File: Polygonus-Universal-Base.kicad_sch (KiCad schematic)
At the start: 11 parts, among them J1 Conn_02x04_Top_Bottom, J4 Polygonus_Plugs, J5 Conn_02x04_Top_Bottom, U1 f042_wideband_module, U14 f042_wideband_module

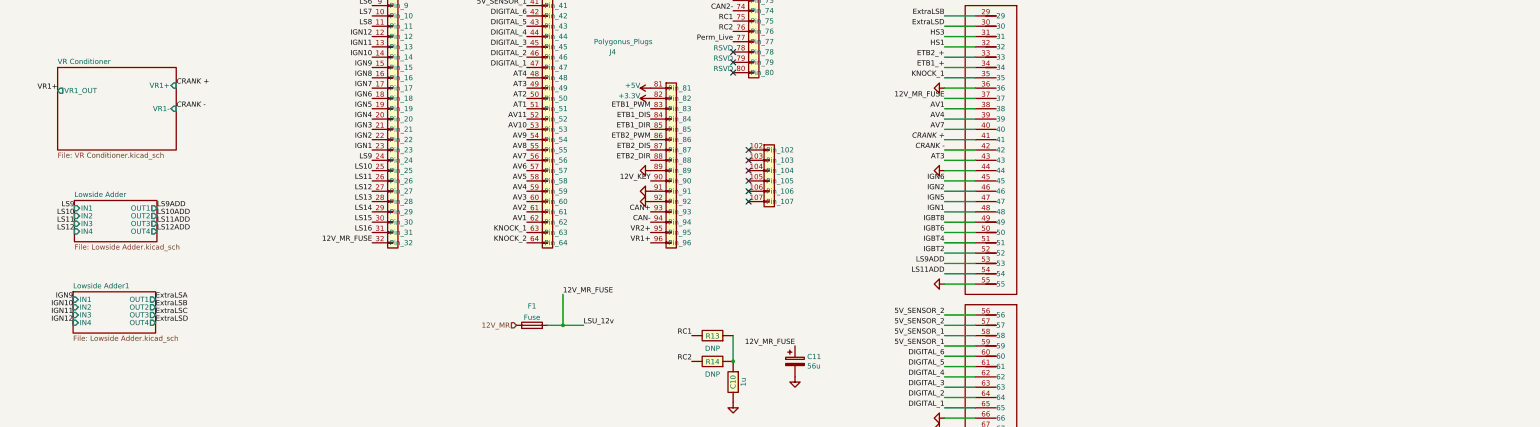
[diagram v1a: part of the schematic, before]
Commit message: Add freewheel diodes, power pins explanation comment
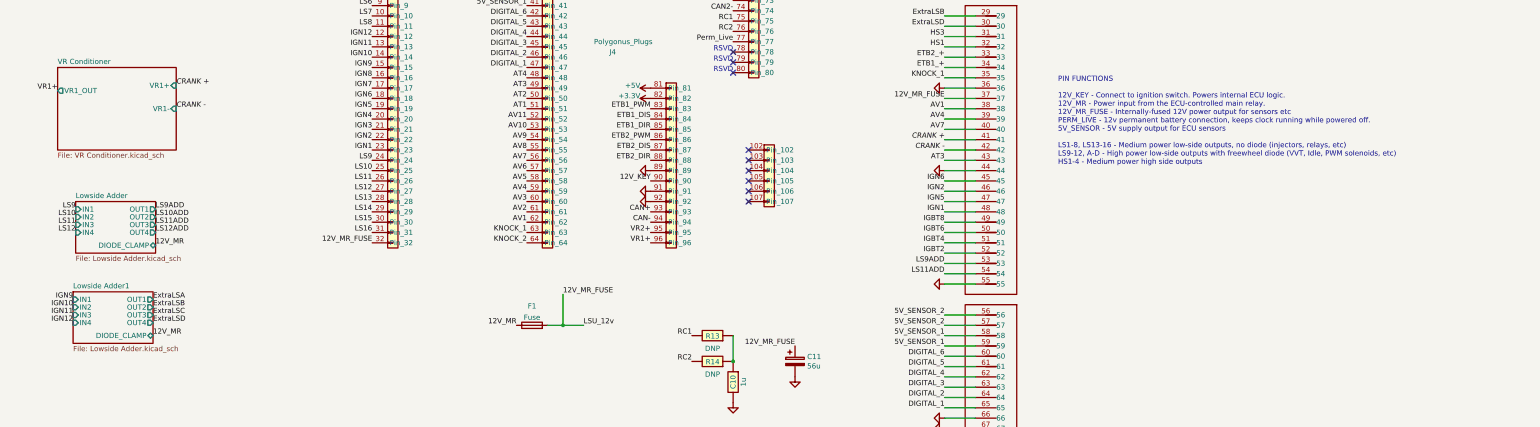
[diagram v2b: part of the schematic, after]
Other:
- sheet Lowside Adder ports: added DIODE_CLAMP; removed none
- sheet Lowside Adder1 ports: added DIODE_CLAMP; removed none
- note added: "PIN FUNCTIONS 12V_KEY - Connect to ignition switch. Powers internal ECU logic. 12V_MR - Power input from the ECU-controlled main relay. 12V_MR_FUSE - Internally-fused 12V power output for sensors etc PERM_LIVE - 12v permanent battery connection, keeps clock running while powered off. 5V_SENSOR - 5V supply output for ECU sensors LS1-8, LS13-16 - Medium power low-side outputs, no diode (injectors, 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"
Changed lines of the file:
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@@
     (stroke (width 0) (type default))
   )
+  (text "PIN FUNCTIONS\n\n12V_KEY - Connect to ignition switch. Powers internal ECU logic.\n12V_MR - Power input from the ECU-controlled main relay.\n12V_MR_FUSE - Internally-fused 12V power output for sensors etc\nPERM_LIVE - 12v permanent battery connection, keeps clock running while powered off.\n5V_SENSOR - 5V supply output for ECU sensors\n\nLS1-8, LS13-16 - Medium power low-side outputs, no diode (injectors, relays, etc)\nLS9-12, A-D - High power low-side outputs with freewheel diode (VVT, Idle, PWM solenoids, etc)\nHS1-4 - Medium power high side outputs"
+    (at 299.72 144.78 0)
+    (effects (font (size 1.27 1.27)) (justify left bottom))
+  )
   (text "RSVD" (at 168.91 97.79 0)
     (effects (font (size 1.27 1.27)) (justify right bottom))
@@
     (effects (font (size 1.27 1.27)) (justify right bottom))
   )
-  (label "LS11" (at 57.4793 159.1204 180) (fields_autoplaced)
+  (label "LS11" (at 57.785 159.385 180) (fields_autoplaced)
     (effects (font (size 1.27 1.27)) (justify right bottom))
   )
@@
     (effects (font (size 1.27 1.27)) (justify right bottom))
   )
-  (label "ExtraLSB" (at 77.47 179.705 0) (fields_autoplaced)
+  (label "ExtraLSB" (at 76.835 179.705 0) (fields_autoplaced)
     (effects (font (size 1.27 1.27)) (justify left bottom))
   )
@@
     (effects (font (size 1.27 1.27)) (justify left bottom))
   )
+  (label "12V_MR" (at 166.37 184.15 180) (fields_autoplaced)
+    (effects (font (size 1.27 1.27)) (justify right bottom))
+  )
   (label "HeaterNeg2" (at 193.04 223.52 0) (fields_autoplaced)
     (effects (font (size 1.27 1.27)) (justify left bottom))
@@
     (effects (font (size 1.27 1.27)) (justify left bottom))
   )
-  (label "LS10ADD" (at 77.7993 157.2154 0) (fields_autoplaced)
+  (label "LS10ADD" (at 77.47 157.48 0) (fields_autoplaced)
     (effects (font (size 1.27 1.27)) (justify left bottom))
   )
@@
     (effects (font (size 1.27 1.27)) (justify right bottom))
   )
-  (label "LS12" (at 57.4793 161.0254 180) (fields_autoplaced)
+  (label "LS12" (at 57.785 161.29 180) (fields_autoplaced)
     (effects (font (size 1.27 1.27)) (justify right bottom))
   )
@@
     (effects (font (size 1.27 1.27)) (justify right bottom))
   )
-  (label "LS9ADD" (at 77.7993 155.3104 0) (fields_autoplaced)
+  (label "LS9ADD" (at 77.47 155.575 0) (fields_autoplaced)
     (effects (font (size 1.27 1.27)) (justify left bottom))
   )
@@
     (effects (font (size 1.27 1.27) italic) (justify right bottom))
   )
-  (label "LS11ADD" (at 77.7993 159.1204 0) (fields_autoplaced)
+  (label "LS11ADD" (at 77.47 159.385 0) (fields_autoplaced)
     (effects (font (size 1.27 1.27)) (justify left bottom))
   )
@@
     (effects (font (size 1.27 1.27)) (justify right bottom))
   )
-  (label "LS12ADD" (at 77.7993 161.0254 0) (fields_autoplaced)
+  (label "LS12ADD" (at 77.47 161.29 0) (fields_autoplaced)
+    (effects (font (size 1.27 1.27)) (justify left bottom))
+  )
+  (label "12V_MR" (at 77.47 164.465 0) (fields_autoplaced)
     (effects (font (size 1.27 1.27)) (justify left bottom))
   )
@@
     (effects (font (size 1.27 1.27)) (justify right bottom))
   )
-  (label "LS9" (at 57.4793 155.3104 180) (fields_autoplaced)
+  (label "LS9" (at 57.785 155.575 180) (fields_autoplaced)
     (effects (font (size 1.27 1.27)) (justify right bottom))
   )
@@
     (effects (font (size 1.27 1.27)) (justify right bottom))
   )
-  (label "ExtraLSD" (at 77.47 183.515 0) (fields_autoplaced)
+  (label "ExtraLSD" (at 76.835 183.515 0) (fields_autoplaced)
     (effects (font (size 1.27 1.27)) (justify left bottom))
   )
@@
     (effects (font (size 1.27 1.27)) (justify right bottom))
   )
-  (label "LS10" (at 57.4793 157.2154 180) (fields_autoplaced)
+  (label "LS10" (at 57.785 157.48 180) (fields_autoplaced)
     (effects (font (size 1.27 1.27)) (justify right bottom))
   )
@@
     (effects (font (size 1.27 1.27)) (justify right bottom))
   )
-  (label "ExtraLSC" (at 77.47 181.61 0) (fields_autoplaced)
+  (label "ExtraLSC" (at 76.835 181.61 0) (fields_autoplaced)
     (effects (font (size 1.27 1.27)) (justify left bottom))
   )
@@
     (effects (font (size 1.27 1.27)) (justify right bottom))
   )
+  (label "12V_MR" (at 76.835 186.69 0) (fields_autoplaced)
+    (effects (font (size 1.27 1.27)) (justify left bottom))
+  )
   (label "IGN11" (at 57.15 181.61 180) (fields_autoplaced)
     (effects (font (size 1.27 1.27)) (justify right bottom))
@@
     (effects (font (size 1.27 1.27)) (justify right bottom))
   )
-  (label "ExtraLSA" (at 77.47 177.8 0) (fields_autoplaced)
+  (label "ExtraLSA" (at 76.835 177.8 0) (fields_autoplaced)
     (effects (font (size 1.27 1.27)) (justify left bottom))
   )
@@
   (label "RC2" (at 219.71 111.76 180) (fields_autoplaced)
     (effects (font (size 1.27 1.27)) (justify right bottom))
-  )
-  (hierarchical_label "12V_MR" (shape input) (at 166.37 184.15 180) (fields_autoplaced)
-    (effects (font (size 1.27 1.27)) (justify right))
   )
   (symbol (lib_name "GND_1") (lib_id "power:GND") (at 219.71 96.52 270) (unit 1)
@@
     )
   )
-  (sheet (at 57.15 175.895) (size 20.32 10.16) (fields_autoplaced)
+  (sheet (at 57.15 175.895) (size 19.685 12.7) (fields_autoplaced)
     (stroke (width 0) (type solid))
     (fill (color 0 0 0 0.0000))
@@
       (effects (font (size 1.27 1.27)) (justify left bottom))
     )
-    (property "Sheetfile" "Lowside Adder.kicad_sch" (at 57.15 186.6396 0)
+    (property "Sheetfile" "Lowside Adder.kicad_sch" (at 57.15 189.1796 0)
       (effects (font (size 1.27 1.27)) (justify left top))
     )
-    (pin "OUT1" output (at 77.47 177.8 0)
-      (effects (font (size 1.27 1.27)) (justify right))
-    )
-    (pin "OUT2" output (at 77.47 179.705 0)
+    (pin "OUT1" output (at 76.835 177.8 0)
+      (effects (font (size 1.27 1.27)) (justify right))
+    )
+    (pin "OUT2" output (at 76.835 179.705 0)
       (effects (font (size 1.27 1.27)) (justify right))
     )
@@
       (effects (font (size 1.27 1.27)) (justify left))
     )
-    (pin "OUT3" output (at 77.47 181.61 0)
-      (effects (font (size 1.27 1.27)) (justify right))
-    )
-    (pin "OUT4" output (at 77.47 183.515 0)
+    (pin "OUT3" output (at 76.835 181.61 0)
+      (effects (font (size 1.27 1.27)) (justify right))
+    )
+    (pin "OUT4" output (at 76.835 183.515 0)
       (effects (font (size 1.27 1.27)) (justify right))
     )
@@
     (pin "IN4" input (at 57.15 183.515 180)
       (effects (font (size 1.27 1.27)) (justify left))
+    )
+    (pin "DIODE_CLAMP" bidirectional (at 76.835 186.69 0)
+      (effects (font (size 1.27 1.27)) (justify right))
     )
     (instances
@@
     )
   )
-  (sheet (at 57.4793 153.4054) (size 20.32 10.16) (fields_autoplaced)
+  (sheet (at 57.785 153.67) (size 19.685 12.7) (fields_autoplaced)
     (stroke (width 0) (type solid))
     (fill (color 0 0 0 0.0000))
-    (property "Sheetname" "Lowside Adder" (at 57.4793 152.6938 0)
+    (property "Sheetname" "Lowside Adder" (at 57.785 152.9584 0)
       (effects (font (size 1.27 1.27)) (justify left bottom))
     )
-    (property "Sheetfile" "Lowside Adder.kicad_sch" (at 57.4793 164.15 0)
+    (property "Sheetfile" "Lowside Adder.kicad_sch" (at 57.785 166.9546 0)
       (effects (font (size 1.27 1.27)) (justify left top))
     )
-    (pin "OUT1" output (at 77.7993 155.3104 0)
-      (effects (font (size 1.27 1.27)) (justify right))
-    )
-    (pin "OUT2" output (at 77.7993 157.2154 0)
-      (effects (font (size 1.27 1.27)) (justify right))
-    )
-    (pin "IN1" input (at 57.4793 155.3104 180)
-      (effects (font (size 1.27 1.27)) (justify left))
-    )
-    (pin "IN2" input (at 57.4793 157.2154 180)
-      (effects (font (size 1.27 1.27)) (justify left))
-    )
-    (pin "OUT3" output (at 77.7993 159.1204 0)
-      (effects (font (size 1.27 1.27)) (justify right))
-    )
-    (pin "OUT4" output (at 77.7993 161.0254 0)
-      (effects (font (size 1.27 1.27)) (justify right))
-    )
-    (pin "IN3" input (at 57.4793 159.1204 180)
-      (effects (font (size 1.27 1.27)) (justify left))
-    )
-    (pin "IN4" input (at 57.4793 161.0254 180)
-      (effects (font (size 1.27 1.27)) (justify left))
-    )
-    (instances
+    (pin "OUT1" output (at 77.47 155.575 0)
+      (effects (font (size 1.27 1.27)) (justify right))
+    )
+    (pin "OUT2" output (at 77.47 157.48 0)
+      (effects (font (size 1.27 1.27)) (justify right))
+    )
+    (pin "IN1" input (at 57.785 155.575 180)
+      (effects (font (size 1.27 1.27)) (justify left))
+    )
+    (pin "IN2" input (at 57.785 157.48 180)
+      (effects (font (size 1.27 1.27)) (justify left))
+    )
+    (pin "OUT3" output (at 77.47 159.385 0)
+      (effects (font (size 1.27 1.27)) (justify right))
+    )
+    (pin "OUT4" output (at 77.47 161.29 0)
+      (effects (font (size 1.27 1.27)) (justify right))
+    )
+    (pin "IN3" input (at 57.785 159.385 180)
+      (effects (font (size 1.27 1.27)) (justify left))
+    )
+    (pin "IN4" input (at 57.785 161.29 180)
+      (effects (font (size 1.27 1.27)) (justify left))
+    )
+    (pin "DIODE_CLAMP" bidirectional (at 77.47 164.465 0)
+      (effects (font (size 1.27 1.27)) (justify right))
+    )
+    (instances

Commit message: route widebands to main connector
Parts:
- removed J1, J5: Conn_02x04_Top_Bottom, Connector_Molex:Molex_Micro-Fit_3.0_43045-0800_2x04_P3.00mm_Horizontal, symbol Connector_Generic:Conn_02x04_Top_Bottom
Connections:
- net IGN1: no longer Motronic_88pin1.48
- net IGN2: no longer Motronic_88pin1.46
- net IGN3: no longer Motronic_88pin1.20
- net IGN4: no longer Motronic_88pin1.18
- net IGN5: no longer Motronic_88pin1.47
- net IGN6: no longer Motronic_88pin1.45
- net IGN7: no longer Motronic_88pin1.19
- net IGN8: no longer Motronic_88pin1.17
- net LSU_Ip: now also Motronic_88pin1.48
- net LSU_Ip2: now also Motronic_88pin1.46
- net LSU_Rtrim: now also Motronic_88pin1.47
- net LSU_Rtrim2: now also Motronic_88pin1.45
- net LSU_Un: now also Motronic_88pin1.19
- net LSU_Un2: now also Motronic_88pin1.17
- net LSU_Vm: now also Motronic_88pin1.20
- net LSU_Vm2: now also Motronic_88pin1.18
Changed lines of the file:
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@@
     (effects (font (size 1.27 1.27)) (justify right bottom))
   )
-  (label "HeaterNeg" (at 76.2 247.65 0) (fields_autoplaced)
+  (label "HeaterNeg" (at 312.42 164.465 0) (fields_autoplaced)
     (effects (font (size 1.27 1.27)) (justify left bottom))
   )
@@
   )
   (label "LS4" (at 271.78 240.03 180) (fields_autoplaced)
-    (effects (font (size 1.27 1.27)) (justify right bottom))
-  )
-  (label "IGN7" (at 271.78 76.2 180) (fields_autoplaced)
     (effects (font (size 1.27 1.27)) (justify right bottom))
   )
@@
     (effects (font (size 1.27 1.27)) (justify right bottom))
   )
-  (label "HeaterNeg" (at 76.2 245.11 0) (fields_autoplaced)
-    (effects (font (size 1.27 1.27)) (justify left bottom))
-  )
   (label "IGBT7" (at 186.69 59.69 0) (fields_autoplaced)
     (effects (font (size 1.27 1.27)) (justify left bottom))
@@
     (effects (font (size 1.27 1.27)) (justify right bottom))
   )
-  (label "LSU_12v" (at 210.82 250.19 180) (fields_autoplaced)
-    (effects (font (size 1.27 1.27)) (justify right bottom))
-  )
   (label "AT1" (at 168.91 130.81 180) (fields_autoplaced)
     (effects (font (size 1.27 1.27)) (justify right bottom))
@@
     (effects (font (size 1.27 1.27)) (justify right bottom))
   )
-  (label "IGN5" (at 271.78 153.67 180) (fields_autoplaced)
-    (effects (font (size 1.27 1.27)) (justify right bottom))
-  )
   (label "LSU_Un2" (at 193.04 236.22 0) (fields_autoplaced)
     (effects (font (size 1.27 1.27)) (justify left bottom))
@@
     (effects (font (size 1.27 1.27)) (justify right bottom))
   )
-  (label "HeaterNeg2" (at 223.52 247.65 0) (fields_autoplaced)
-    (effects (font (size 1.27 1.27)) (justify left bottom))
-  )
   (label "LS10ADD" (at 77.47 157.48 0) (fields_autoplaced)
     (effects (font (size 1.27 1.27)) (justify left bottom))
@@
     (effects (font (size 1.27 1.27)) (justify right bottom))
   )
-  (label "LSU_Rtrim" (at 76.2 252.73 0) (fields_autoplaced)
-    (effects (font (size 1.27 1.27)) (justify left bottom))
-  )
-  (label "LSU_Rtrim2" (at 223.52 255.27 0) (fields_autoplaced)
-    (effects (font (size 1.27 1.27)) (justify left bottom))
-  )
-  (label "LSU_Un2" (at 210.82 255.27 180) (fields_autoplaced)
+  (label "LSU_Rtrim" (at 271.78 153.67 180) (fields_autoplaced)
+    (effects (font (size 1.27 1.27)) (justify right bottom))
+  )
+  (label "LSU_Rtrim2" (at 271.78 148.59 180) (fields_autoplaced)
+    (effects (font (size 1.27 1.27)) (justify right bottom))
+  )
+  (label "LSU_Un2" (at 271.78 71.12 180) (fields_autoplaced)
     (effects (font (size 1.27 1.27)) (justify right bottom))
   )
@@
     (effects (font (size 1.27 1.27)) (justify right bottom))
   )
-  (label "LSU_Vm2" (at 223.52 252.73 0) (fields_autoplaced)
-    (effects (font (size 1.27 1.27)) (justify left bottom))
+  (label "LSU_Vm2" (at 271.78 73.66 180) (fields_autoplaced)
+    (effects (font (size 1.27 1.27)) (justify right bottom))
   )
   (label "12V_MR_FUSE" (at 130.81 163.83 180) (fields_autoplaced)
@@
     (effects (font (size 1.27 1.27)) (justify right bottom))
   )
-  (label "IGN2" (at 271.78 151.13 180) (fields_autoplaced)
-    (effects (font (size 1.27 1.27)) (justify right bottom))
-  )
   (label "AV1" (at 168.91 158.75 180) (fields_autoplaced)
     (effects (font (size 1.27 1.27)) (justify right bottom))
@@
     (effects (font (size 1.27 1.27)) (justify right bottom))
   )
-  (label "LSU_12v" (at 63.5 247.65 180) (fields_autoplaced)
-    (effects (font (size 1.27 1.27)) (justify right bottom))
-  )
   (label "RC1" (at 209.55 186.69 180) (fields_autoplaced)
     (effects (font (size 1.27 1.27)) (justify right bottom))
@@
     (effects (font (size 1.27 1.27)) (justify right bottom))
   )
-  (label "LSU_12v" (at 63.5 245.11 180) (fields_autoplaced)
-    (effects (font (size 1.27 1.27)) (justify right bottom))
-  )
   (label "HS4" (at 219.71 83.82 180) (fields_autoplaced)
     (effects (font (size 1.27 1.27)) (justify right bottom))
@@
     (effects (font (size 1.27 1.27)) (justify right bottom))
   )
-  (label "HeaterNeg2" (at 223.52 250.19 0) (fields_autoplaced)
-    (effects (font (size 1.27 1.27)) (justify left bottom))
-  )
-  (label "LSU_Vm" (at 76.2 250.19 0) (fields_autoplaced)
-    (effects (font (size 1.27 1.27)) (justify left bottom))
+  (label "HeaterNeg2" (at 315.595 170.18 0) (fields_autoplaced)
+    (effects (font (size 1.27 1.27)) (justify left bottom))
+  )
+  (label "LSU_Vm" (at 271.78 78.74 180) (fields_autoplaced)
+    (effects (font (size 1.27 1.27)) (justify right bottom))
   )
   (label "DIGITAL_2" (at 168.91 118.11 180) (fields_autoplaced)
@@
   )
   (label "12V_MR_FUSE" (at 271.78 53.34 180) (fields_autoplaced)
-    (effects (font (size 1.27 1.27)) (justify right bottom))
-  )
-  (label "IGN3" (at 271.78 78.74 180) (fields_autoplaced)
     (effects (font (size 1.27 1.27)) (justify right bottom))
   )
@@
     (effects (font (size 1.27 1.27)) (justify left bottom))
   )
-  (label "IGN6" (at 271.78 148.59 180) (fields_autoplaced)
-    (effects (font (size 1.27 1.27)) (justify right bottom))
-  )
   (label "IGBT5" (at 186.69 54.61 0) (fields_autoplaced)
     (effects (font (size 1.27 1.27)) (justify left bottom))
@@
     (effects (font (size 1.27 1.27)) (justify right bottom))
   )
-  (label "IGN4" (at 271.78 73.66 180) (fields_autoplaced)
-    (effects (font (size 1.27 1.27)) (justify right bottom))
-  )
   (label "IGN6" (at 130.81 128.27 180) (fields_autoplaced)
     (effects (font (size 1.27 1.27)) (justify right bottom))
@@
     (effects (font (size 1.27 1.27)) (justify right bottom))
   )
-  (label "LSU_Ip2" (at 210.82 252.73 180) (fields_autoplaced)
+  (label "LSU_Ip2" (at 271.78 151.13 180) (fields_autoplaced)
     (effects (font (size 1.27 1.27)) (justify right bottom))
   )
@@
     (effects (font (size 1.27 1.27)) (justify right bottom))
   )
-  (label "IGN8" (at 271.78 71.12 180) (fields_autoplaced)
-    (effects (font (size 1.27 1.27)) (justify right bottom))
-  )
   (label "LS3" (at 130.81 97.79 180) (fields_autoplaced)
     (effects (font (size 1.27 1.27)) (justify right bottom))
@@
     (effects (font (size 1.27 1.27)) (justify left bottom))
   )
-  (label "IGN1" (at 271.78 156.21 180) (fields_autoplaced)
-    (effects (font (size 1.27 1.27)) (justify right bottom))
-  )
   (label "CAN_TX2" (at 162.56 226.06 180) (fields_autoplaced)
     (effects (font (size 1.27 1.27)) (justify right bottom))
@@
     (effects (font (size 1.27 1.27)) (justify right bottom))
   )
-  (label "LSU_12v" (at 210.82 247.65 180) (fields_autoplaced)
-    (effects (font (size 1.27 1.27)) (justify right bottom))
-  )
   (label "12V_MR_FUSE" (at 271.78 212.09 180) (fields_autoplaced)
     (effects (font (size 1.27 1.27)) (justify right bottom))
@@
     (effects (font (size 1.27 1.27)) (justify right bottom))
   )
-  (label "LSU_Un" (at 63.5 252.73 180) (fields_autoplaced)
+  (label "LSU_Un" (at 271.78 76.2 180) (fields_autoplaced)
     (effects (font (size 1.27 1.27)) (justify right bottom))
   )
@@
     (effects (font (size 1.27 1.27)) (justify right bottom))
   )
-  (label "LSU_Ip" (at 63.5 250.19 180) (fields_autoplaced)
+  (label "LSU_Ip" (at 271.78 156.21 180) (fields_autoplaced)
     (effects (font (size 1.27 1.27)) (justify right bottom))
   )
@@
     )
   )
-  (symbol (lib_id "Connector_Generic:Conn_02x04_Top_Bottom") (at 68.58 247.65 0) (unit 1)
-    (in_bom yes) (on_board yes) (dnp no) (fields_autoplaced)
-    (property "Reference" "J5" (at 69.85 238.76 0)
-      (effects (font (size 1.27 1.27)))
-    )
-    (property "Value" "Conn_02x04_Top_Bottom" (at 69.85 241.3 0)
-      (effects (font (size 1.27 1.27)))
-    )
-    (property "Footprint" "Connector_Molex:Molex_Micro-Fit_3.0_43045-0800_2x04_P3.00mm_Horizontal" (at 68.58 247.65 0)
-      (effects (font (size 1.27 1.27)) hide)
-    )
-    (property "Datasheet" "~" (at 68.58 247.65 0)
-      (effects (font (size 1.27 1.27)) hide)
-    )
-    (pin "1")
-    (pin "2")
-    (pin "3")
-    (pin "4")
-    (pin "5")
-    (pin "6")
-    (pin "7")
-    (pin "8")
-    (instances
-      (project "Polygonus-Universal-Base"
-        (path "/e63e39d7-6ac0-4ffd-8aa3-1841a4541b55"
-          (reference "J5") (unit 1)
-        )
-      )
-    )
-  )
   (symbol (lib_id "Wideband:f042_wideband_module") (at 177.8 232.41 0) (unit 1)
     (in_bom yes) (on_board yes) (dnp no) (fields_autoplaced)
@@
         )
       )
-    )
-  )
-  (symbol (lib_id "Connector_Generic:Conn_02x04_Top_Bottom") (at 215.9 250.19 0) (unit 1)
-    (in_bom yes) (on_board yes) (dnp no) (fields_autoplaced)
-    (property "Reference" "J1" (at 217.17 241.3 0)
-      (effects (font (size 1.27 1.27)))
-    )
-    (property "Value" "Conn_02x04_Top_Bottom" (at 217.17 243.84 0)
-      (effects (font (size 1.27 1.27)))
-    )
-    (property "Footprint" "Connector_Molex:Molex_Micro-Fit_3.0_43045-0800_2x04_P3.00mm_Horizontal" (at 215.9 250.19 0)
-      (effects (font (size 1.27 1.27)) hide)
-    )
-    (property "Datasheet" "~" (at 215.9 250.19 0)
-      (effects (font (size 1.27 1.27)) hide)
-    )
-    (pin "1")
-    (pin "2")
-    (pin "3")
-    (pin "4")
-    (pin "5")
-    (pin "6")
-    (pin "7")
-    (pin "8")
-    (instances
-      (project "Polygonus-Universal-Base"
-        (path "/e63e39d7-6ac0-4ffd-8aa3-1841a4541b55"
-          (reference "J1") (unit 1)
-        )
-      )
